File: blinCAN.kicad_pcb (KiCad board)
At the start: 2 copper layers, 127.1 x 67.1 mm, 88 parts, among them IC201 ATMEGA328P-AU, J501 Conn_Address, P101 Conn_PWR_IN, P102 Conn_PWR_IN, P103 CONN_ICSP, P104 USB B, P105 Conn_CAN, P106 Conn_CAN, P601 D-SUB 25, P602 D-SUB 25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

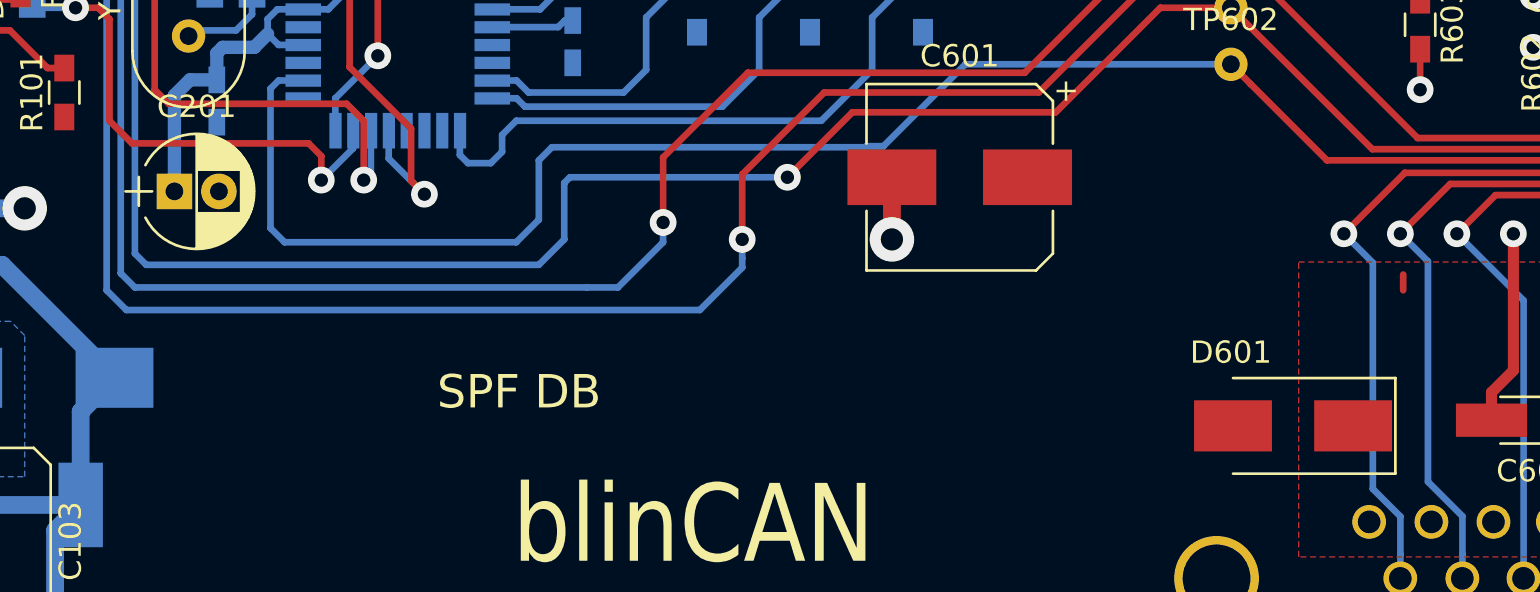
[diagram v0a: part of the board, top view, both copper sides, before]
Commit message: Add symbols to PCB.
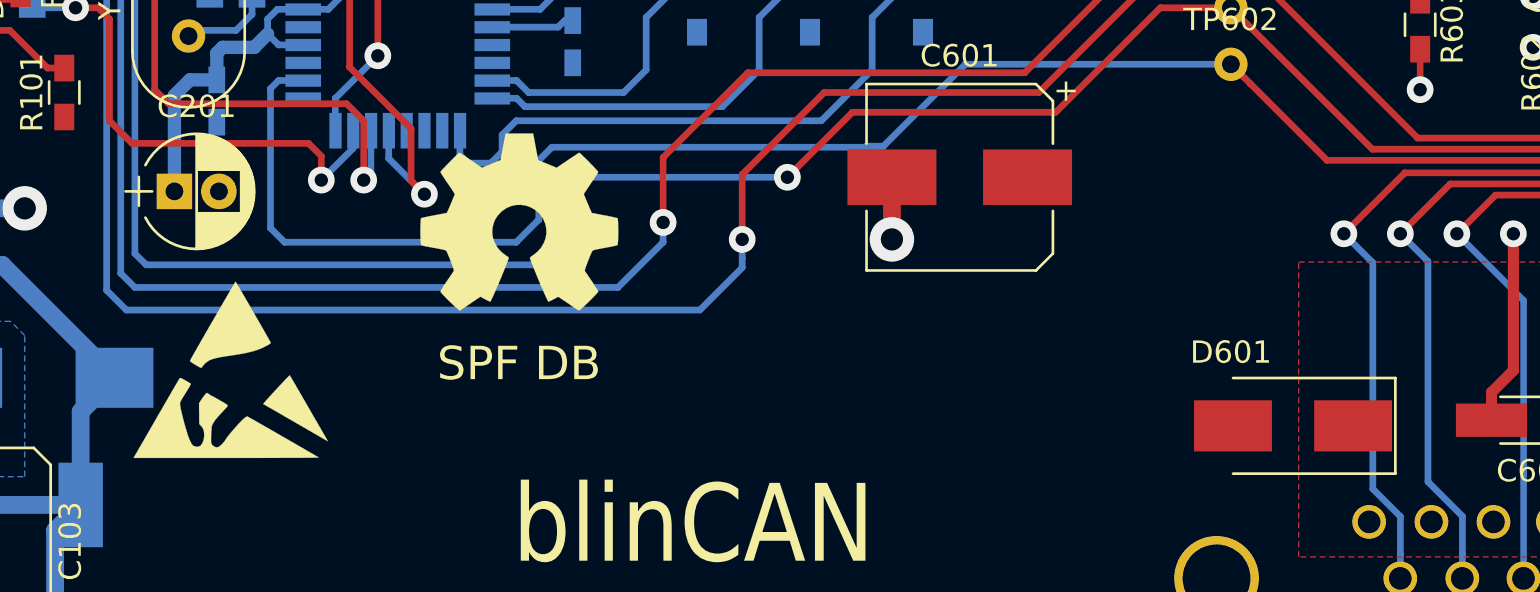
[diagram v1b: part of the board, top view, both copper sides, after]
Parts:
- added REF***: OSHW-Symbol_8.9x8mm_SilkScreen, Symbols:OSHW-Symbol_8.9x8mm_SilkScreen, F.Cu at (77.1, 88.4)
- added REF***: ESD-Logo_8.9x8mm_SilkScreen, Symbols:ESD-Logo_8.9x8mm_SilkScreen, F.Cu at (64.1, 95.0)
- added REF***: KiCad-Logo2_8mm_SilkScreen, Symbols:KiCad-Logo2_8mm_SilkScreen, B.Cu at (94.9, 97.3)
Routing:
- net (no net): track 0.71 -> 0.00 mm

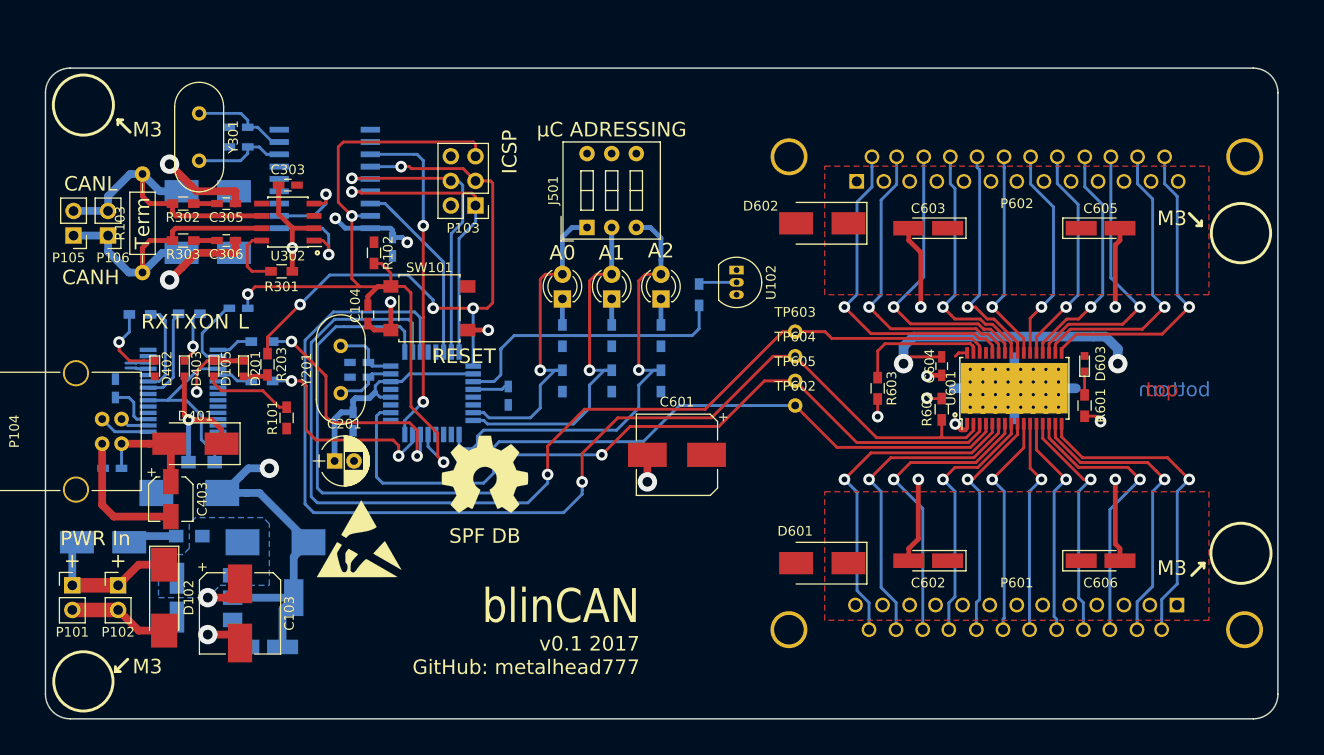
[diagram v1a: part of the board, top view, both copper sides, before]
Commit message: Add mounting holes. Moved symbols.
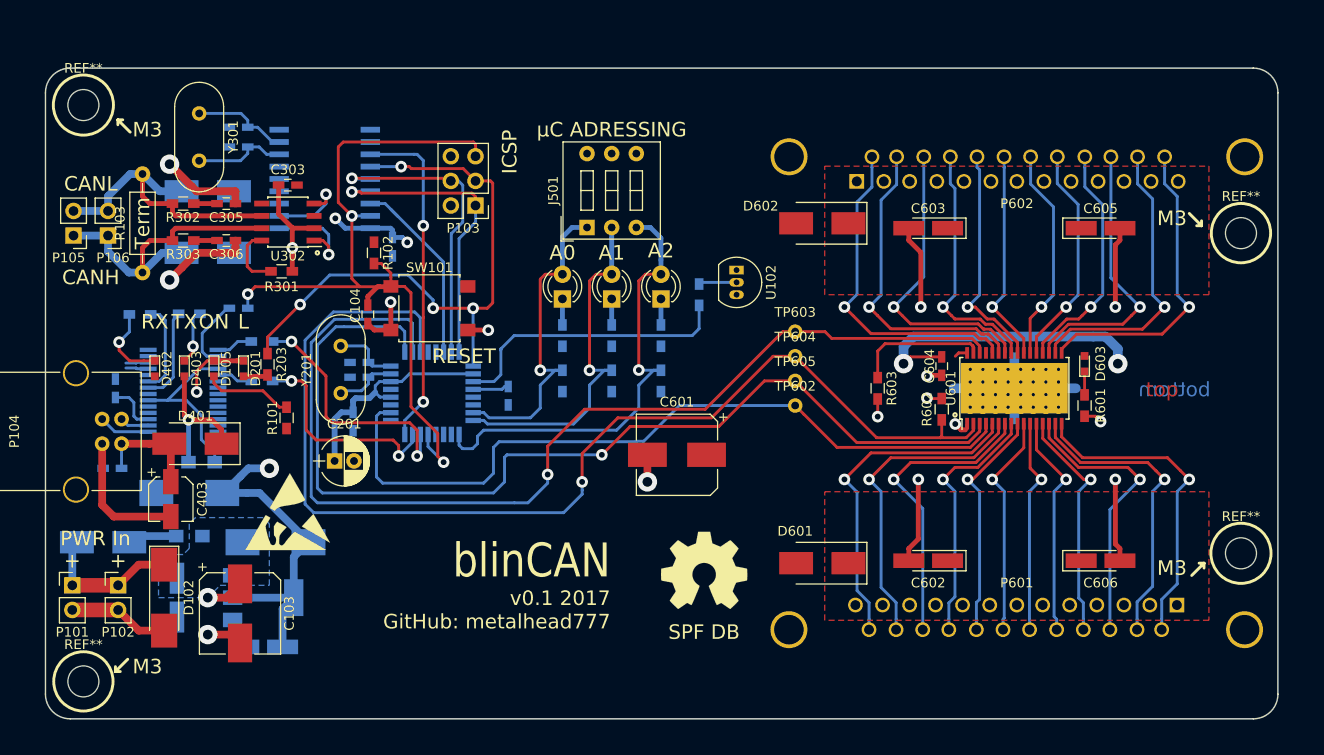
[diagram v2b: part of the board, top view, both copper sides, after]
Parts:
- added REF**: MountingHole_3.2mm_M3_DIN965, Mounting_Holes:MountingHole_3.2mm_M3_DIN965, F.Cu at (155.1, 96.5)
- added REF**: MountingHole_3.2mm_M3_DIN965, Mounting_Holes:MountingHole_3.2mm_M3_DIN965, F.Cu at (155.1, 63.5)
- added REF**: MountingHole_3.2mm_M3_DIN965, Mounting_Holes:MountingHole_3.2mm_M3_DIN965, F.Cu at (35.7, 50.3)
- added REF**: MountingHole_3.2mm_M3_DIN965, Mounting_Holes:MountingHole_3.2mm_M3_DIN965, F.Cu at (35.7, 109.7)
- moved REF*** 24.7 mm to (99.7, 98.3)
- moved REF*** 7.88 mm to (56.8, 92.2)
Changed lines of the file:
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@@
     (tracks 816)
     (zones 0)
-    (modules 91)
+    (modules 95)
     (nets 108)
   )
@@
     (uvia_drill 0.1)
   )
+  (module Mounting_Holes:MountingHole_3.2mm_M3_DIN965 (layer F.Cu)
+    (at 155.067 96.52)
+    (descr "Mounting Hole 3.2mm, no annular, M3, DIN965")
+    (tags "mounting hole 3.2mm no annular m3 din965")
+    (attr virtual)
+    (fp_text reference REF** (at 0 -3.8) (layer F.SilkS)
+      (effects (font (size 1 1) (thickness 0.15)))
+    )
+    (fp_text value MountingHole_3.2mm_M3_DIN965 (at 0 3.8) (layer F.Fab)
+      (effects (font (size 1 1) (thickness 0.15)))
+    )
+    (fp_text user %R (at 0.3 0) (layer F.Fab)
+      (effects (font (size 1 1) (thickness 0.15)))
+    )
+    (fp_circle (center 0 0) (end 2.8 0) (layer Cmts.User) (width 0.15))
+    (fp_circle (center 0 0) (end 3.05 0) (layer F.CrtYd) (width 0.05))
+    (pad 1 np_thru_hole circle (at 0 0) (size 3.2 3.2) (drill 3.2) (layers *.Cu *.Mask))
+  )
+  (module Mounting_Holes:MountingHole_3.2mm_M3_DIN965 (layer F.Cu)
+    (at 155.067 63.5)
+    (descr "Mounting Hole 3.2mm, no annular, M3, DIN965")
+    (tags "mounting hole 3.2mm no annular m3 din965")
+    (attr virtual)
+    (fp_text reference REF** (at 0 -3.8) (layer F.SilkS)
+      (effects (font (size 1 1) (thickness 0.15)))
+    )
+    (fp_text value MountingHole_3.2mm_M3_DIN965 (at 0 3.8) (layer F.Fab)
+      (effects (font (size 1 1) (thickness 0.15)))
+    )
+    (fp_text user %R (at 0.3 0) (layer F.Fab)
+      (effects (font (size 1 1) (thickness 0.15)))
+    )
+    (fp_circle (center 0 0) (end 2.8 0) (layer Cmts.User) (width 0.15))
+    (fp_circle (center 0 0) (end 3.05 0) (layer F.CrtYd) (width 0.05))
+    (pad 1 np_thru_hole circle (at 0 0) (size 3.2 3.2) (drill 3.2) (layers *.Cu *.Mask))
+  )
+  (module Mounting_Holes:MountingHole_3.2mm_M3_DIN965 (layer F.Cu)
+    (at 35.687 50.292)
+    (descr "Mounting Hole 3.2mm, no annular, M3, DIN965")
+    (tags "mounting hole 3.2mm no annular m3 din965")
+    (attr virtual)
+    (fp_text reference REF** (at 0 -3.8) (layer F.SilkS)
+      (effects (font (size 1 1) (thickness 0.15)))
+    )
+    (fp_text value MountingHole_3.2mm_M3_DIN965 (at 0 3.8) (layer F.Fab)
+      (effects (font (size 1 1) (thickness 0.15)))
+    )
+    (fp_text user %R (at 0.3 0) (layer F.Fab)
+      (effects (font (size 1 1) (thickness 0.15)))
+    )
+    (fp_circle (center 0 0) (end 2.8 0) (layer Cmts.User) (width 0.15))
+    (fp_circle (center 0 0) (end 3.05 0) (layer F.CrtYd) (width 0.05))
+    (pad 1 np_thru_hole circle (at 0 0) (size 3.2 3.2) (drill 3.2) (layers *.Cu *.Mask))
+  )
   (module Capacitors_SMD:C_0603_HandSoldering (layer B.Cu)
     (at 51.689 71.247)
@@
   )
   (module Symbols:OSHW-Symbol_8.9x8mm_SilkScreen (layer F.Cu)
-    (at 77.089 88.392)
+    (at 99.695 98.298)
     (descr "Open Source Hardware Symbol")
     (tags "Logo Symbol OSHW")
@@
   )
   (module Symbols:ESD-Logo_8.9x8mm_SilkScreen (layer F.Cu)
-    (at 64.135 94.996)
+    (at 56.769 92.202)
     (descr "Electrostatic discharge Logo")
     (tags "Logo ESD")
@@
       (xy -3.378078 3.914132) (xy -3.267907 3.950347) (xy -3.164549 3.964027) (xy -3.02624 3.958707)) (layer B.SilkS) (width 0.01))
   )
+  (module Mounting_Holes:MountingHole_3.2mm_M3_DIN965 (layer F.Cu)
+    (at 35.687 109.728)
+    (descr "Mounting Hole 3.2mm, no annular, M3, DIN965")
+    (tags "mounting hole 3.2mm no annular m3 din965")
+    (attr virtual)
+    (fp_text reference REF** (at 0 -3.8) (layer F.SilkS)
+      (effects (font (size 1 1) (thickness 0.15)))
+    )
+    (fp_text value MountingHole_3.2mm_M3_DIN965 (at 0 3.8) (layer F.Fab)
+      (effects (font (size 1 1) (thickness 0.15)))
+    )
+    (fp_text user %R (at 0.3 0) (layer F.Fab)
+      (effects (font (size 1 1) (thickness 0.15)))
+    )
+    (fp_circle (center 0 0) (end 2.8 0) (layer Cmts.User) (width 0.15))
+    (fp_circle (center 0 0) (end 3.05 0) (layer F.CrtYd) (width 0.05))
+    (pad 1 np_thru_hole circle (at 0 0) (size 3.2 3.2) (drill 3.2) (layers *.Cu *.Mask))
+  )
   (gr_circle (center 125.5776 82.243395) (end 125.7046 82.370395) (layer F.SilkS) (width 0.2))
-  (gr_text "SPF DB " (at 77.089 94.742) (layer F.SilkS)
+  (gr_text "SPF DB " (at 99.695 104.648) (layer F.SilkS)
     (effects (font (size 1.5 1.5) (thickness 0.3)))
   )
@@
     (effects (font (size 1.5 1.5) (thickness 0.3)))
   )
-  (gr_text blinCAN (at 93.0656 101.981) (layer F.SilkS)
-    (effects (font (size 3.5 3) (thickness 0.4)) (justify right))
+  (gr_text blinCAN (at 90.043 97.282) (layer F.SilkS)
+    (effects (font (size 3.5 3) (thickness 0.6)) (justify right))
   )
-  (gr_text "v0.1 2017\nGitHub: metalhead777" (at 93.0656 107.061) (layer F.SilkS)
+  (gr_text "v0.1 2017\nGitHub: metalhead777" (at 90.043 102.362) (layer F.SilkS)
     (effects (font (size 1.5 1.5) (thickness 0.3)) (justify right))
   )

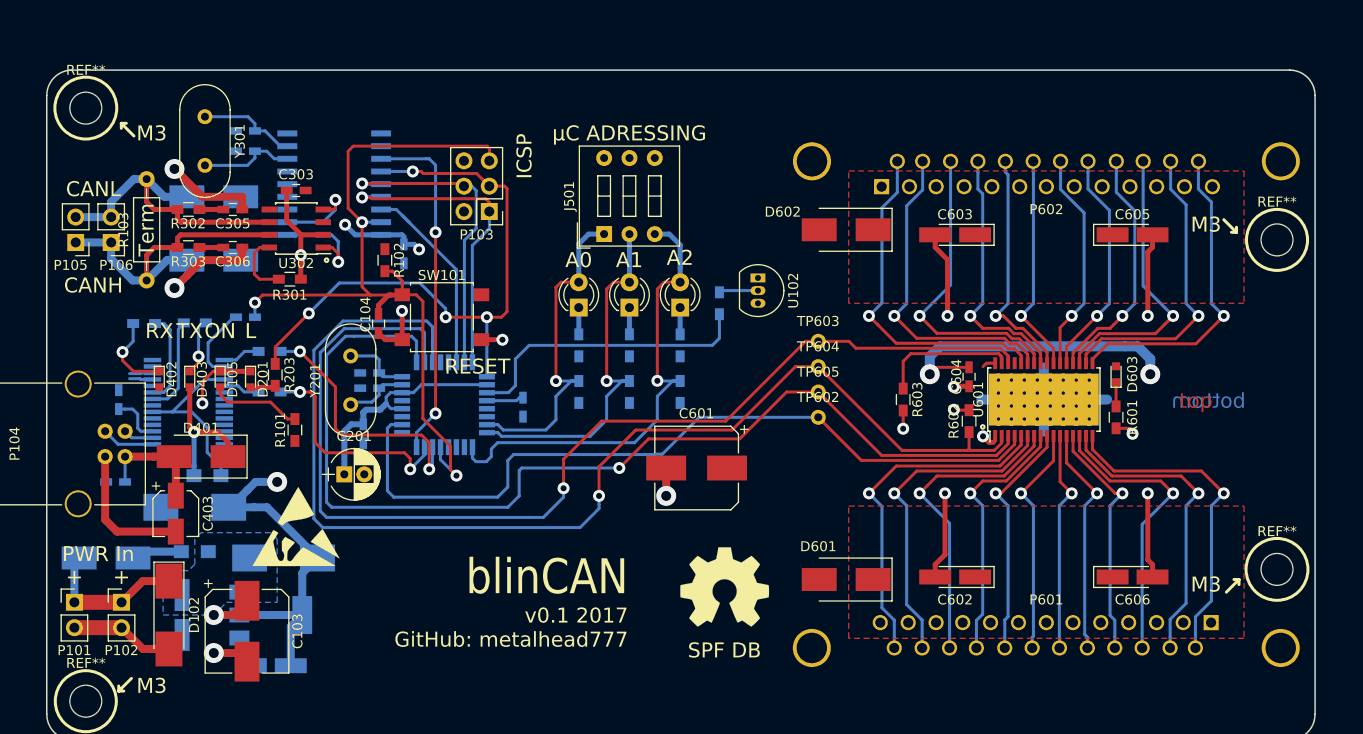
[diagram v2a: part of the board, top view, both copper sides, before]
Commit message: Move symbols.
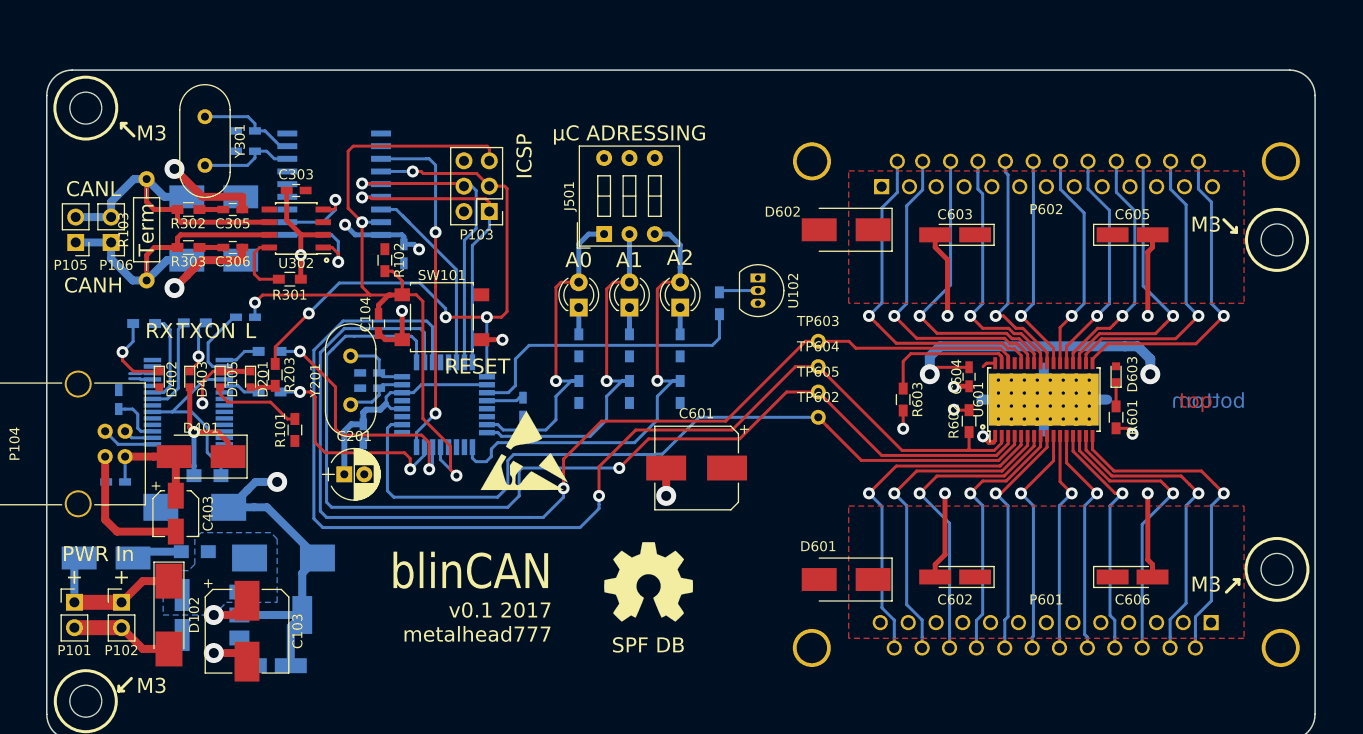
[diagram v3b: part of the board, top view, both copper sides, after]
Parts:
- moved REF*** 24.1 mm to (79.6, 84.6)
- moved REF*** 12.7 mm to (82.2, 97.3)
- moved REF*** 7.64 mm to (92.1, 97.8)
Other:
- board text added: "github.com/metalhead777/blinCAN"
- board text added: "v0.1 2017 metalhead777"
- board text removed: "v0.1 2017 GitHub: metalhead777"
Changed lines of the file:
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@@
     (area 31.700399 46.406999 158.952001 113.663801)
     (thickness 1.6)
-    (drawings 54)
+    (drawings 55)
     (tracks 816)
     (zones 0)
@@
     (tags "mounting hole 3.2mm no annular m3 din965")
     (attr virtual)
-    (fp_text reference REF** (at 0 -3.8) (layer F.SilkS)
+    (fp_text reference REF** (at 0 -3.8) (layer F.SilkS) hide
       (effects (font (size 1 1) (thickness 0.15)))
     )
@@
     (tags "mounting hole 3.2mm no annular m3 din965")
     (attr virtual)
-    (fp_text reference REF** (at 0 -3.8) (layer F.SilkS)
+    (fp_text reference REF** (at 0 -3.8) (layer F.SilkS) hide
       (effects (font (size 1 1) (thickness 0.15)))
     )
@@
     (tags "mounting hole 3.2mm no annular m3 din965")
     (attr virtual)
-    (fp_text reference REF** (at 0 -3.8) (layer F.SilkS)
+    (fp_text reference REF** (at 0 -3.8) (layer F.SilkS) hide
       (effects (font (size 1 1) (thickness 0.15)))
     )
@@
   )
   (module Symbols:OSHW-Symbol_8.9x8mm_SilkScreen (layer F.Cu)
-    (at 99.695 98.298)
+    (at 92.075 97.79)
     (descr "Open Source Hardware Symbol")
     (tags "Logo Symbol OSHW")
@@
   )
   (module Symbols:ESD-Logo_8.9x8mm_SilkScreen (layer F.Cu)
-    (at 56.769 92.202)
+    (at 79.629 84.582)
     (descr "Electrostatic discharge Logo")
     (tags "Logo ESD")
@@
   )
   (module Symbols:KiCad-Logo2_8mm_SilkScreen (layer B.Cu)
-    (at 94.869 97.282 180)
+    (at 82.169 97.282 180)
     (descr "KiCad Logo")
     (tags "Logo KiCad")
@@
     (tags "mounting hole 3.2mm no annular m3 din965")
     (attr virtual)
-    (fp_text reference REF** (at 0 -3.8) (layer F.SilkS)
+    (fp_text reference REF** (at 0 -3.8) (layer F.SilkS) hide
       (effects (font (size 1 1) (thickness 0.15)))
     )
@@
     (pad 1 np_thru_hole circle (at 0 0) (size 3.2 3.2) (drill 3.2) (layers *.Cu *.Mask))
   )
+  (gr_text github.com/metalhead777/blinCAN (at 82.169 104.902) (layer B.SilkS)
+    (effects (font (size 1.5 1.5) (thickness 0.3)) (justify mirror))
+  )
   (gr_circle (center 125.5776 82.243395) (end 125.7046 82.370395) (layer F.SilkS) (width 0.2))
-  (gr_text "SPF DB " (at 99.695 104.648) (layer F.SilkS)
+  (gr_text "SPF DB " (at 92.075 104.14) (layer F.SilkS)
     (effects (font (size 1.5 1.5) (thickness 0.3)))
   )
@@
     (effects (font (size 1.5 1.5) (thickness 0.3)))
   )
-  (gr_text blinCAN (at 90.043 97.282) (layer F.SilkS)
+  (gr_text blinCAN (at 82.423 96.774) (layer F.SilkS)
     (effects (font (size 3.5 3) (thickness 0.6)) (justify right))
   )
-  (gr_text "v0.1 2017\nGitHub: metalhead777" (at 90.043 102.362) (layer F.SilkS)
+  (gr_text "v0.1 2017\nmetalhead777" (at 82.423 101.854) (layer F.SilkS)
     (effects (font (size 1.5 1.5) (thickness 0.3)) (justify right))
   )
